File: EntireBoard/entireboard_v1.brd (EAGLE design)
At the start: 160 x 100 mm, 26 parts, among them U2 RHD2216_QFN

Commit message: add connector, crystals, bom, lbr
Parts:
- added 38.768KHZ: EPSON_32.768KHZ_CRYSTAL, AxonMobile:2-SMD
- added 48MHZ: NDK_48MHZ_CRYSTAL, AxonMobile:4-SMD
- added C18, C19: 12pF, adafruit:C0402
- added C20: 0.1uF, adafruit:C0402
- added J1: FTSH-105-01-XXX-DV-K, AxonMobile:FTSH-105-01-XXX-DV-K
- added R1: 100k, AxonMobile:R0402
- L1, L3, L4, L5, L6: device rcl:0204/5 -> AxonMobile:RHD2000_EVAL_BOARD_0805
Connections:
- removed net DIO5/JTAG_TDO: CC2652R1.10
- removed net DIO6/JTAG_TDI: CC2652R1.11
- new net JTAG_TDI: CC2652R1.27, J1.8
- new net JTAG_TDO: CC2652R1.26, J1.6
- new net N$10: 38.768KHZ.P$2, C19.1, CC2652R1.4
- new net N$3: 48MHZ.P$1, CC2652R1.47
- new net N$4: 48MHZ.P$3, CC2652R1.46
- new net N$5: 38.768KHZ.P$1, C18.1, CC2652R1.3
- new net WMCU_RESET: C20.1, CC2652R1.35, J1.10, R1.1
- net GND: now also 48MHZ.P$2, 48MHZ.P$4, C17.2, C18.2, C19.2, C20.2, CC2652R1.EGP, J1.3, J1.5, J1.9; no longer C17.1, CC2652R1.ETP
- net JTAG_TCK: now also J1.4
- net JTAG_TMS: now also J1.2
- net N$1: now also C17.1; no longer C17.2
- net VDDS: now also R1.2

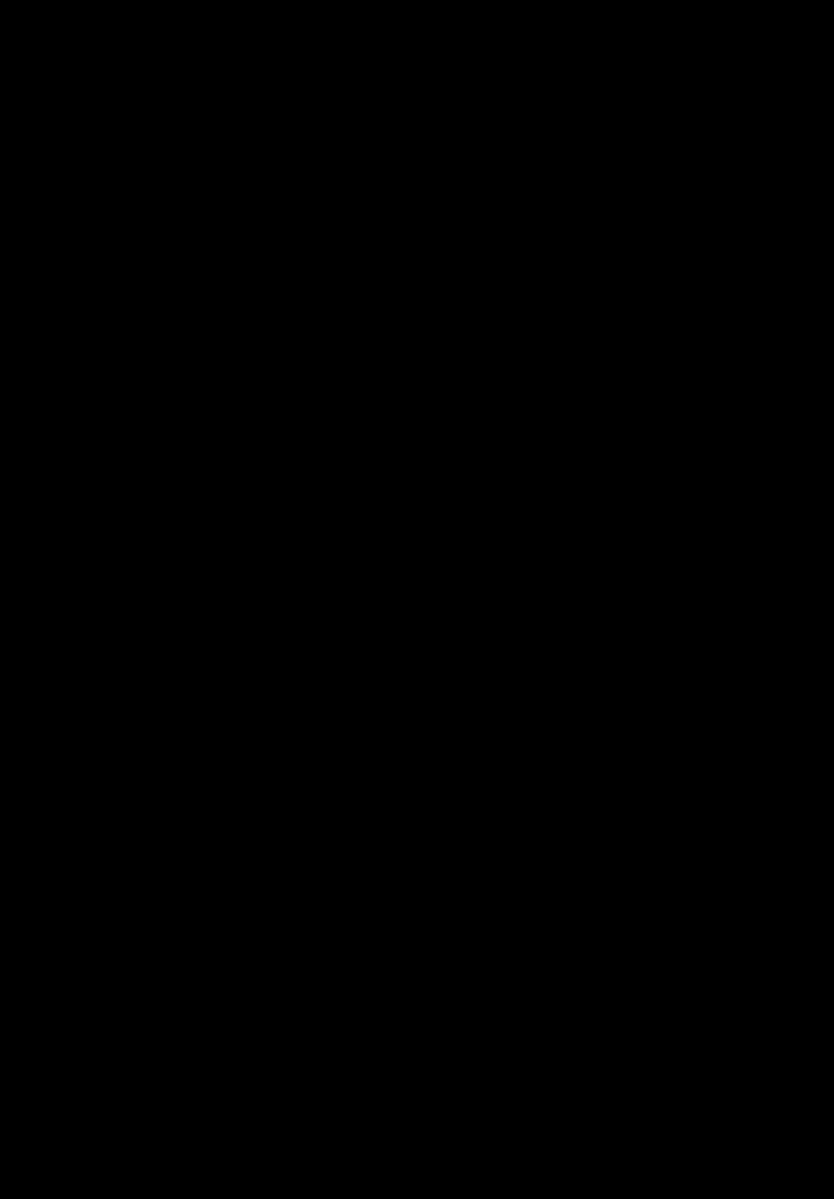
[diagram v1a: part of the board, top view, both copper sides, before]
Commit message: add headers, testpads, current sense resistors, led
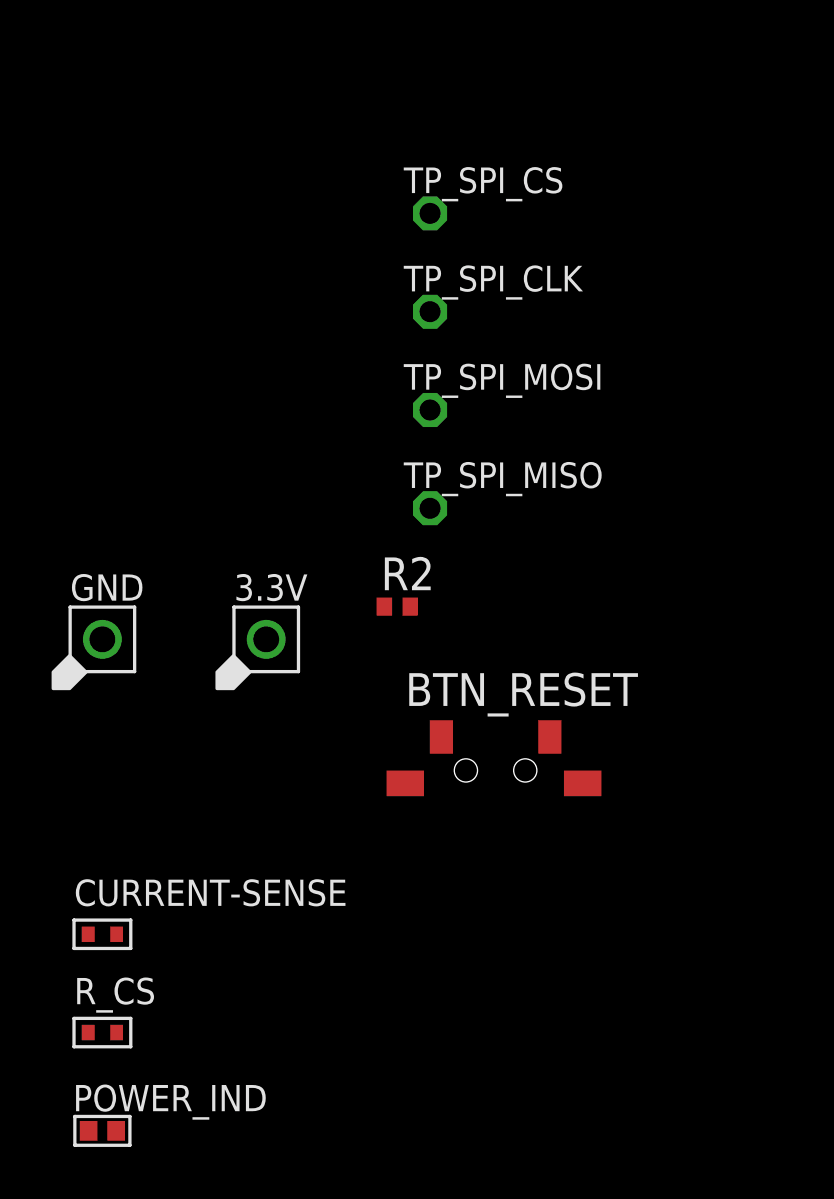
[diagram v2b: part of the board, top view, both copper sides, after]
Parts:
- added 3.3V, GND: MF-CON-2.54mm-01x01, AxonMobile:PTH_2.54MM_01X01
- added BTN_RESET: SW_1188E, AxonMobile:SW_1188E
- added CURRENT-SENSE, R_CS: 0.01ohm, MF_Passives:R0402
- added POWER_IND: LED-SMD, AxonMobile:RHD2000_EVAL_BOARD_0402
- added R2: (no value), AxonMobile:R0402
- added TP_SPI_CLK, TP_SPI_CS, TP_SPI_MISO, TP_SPI_MOSI: RHD2000_EVAL_BOARD_TESTPOINT_SMALL, AxonMobile:RHD2000_EVAL_BOARD_TESTPOINT_SMALL
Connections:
- removed net SPI_CS: CC2652R1.12, U2.19
- new net N$11: C11.2, CURRENT-SENSE.P$1
- new net N$13: POWER_IND.1, R_CS.P$2
- new net N$16: BTN_RESET.P$4, R2.2
- new net SPI_CS_TP: CC2652R1.12, TP_SPI_CS.1, U2.19
- net GND: now also BTN_RESET.P$1, BTN_RESET.P$2, BTN_RESET.P$3, GND.P$1
- net N$2: now also CURRENT-SENSE.P$2; no longer C11.2
- net SPI_CLK: now also TP_SPI_CLK.1
- net SPI_MISO: now also TP_SPI_MISO.1
- net SPI_MOSI: now also TP_SPI_MOSI.1
- net VDDS: now also POWER_IND.2, R_CS.P$1
- net WMCU_RESET: now also R2.1
- net WMCU_VDD: now also 3.3V.P$1
